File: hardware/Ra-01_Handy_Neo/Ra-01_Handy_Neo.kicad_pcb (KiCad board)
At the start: 2 copper layers, 68.6 x 53.3 mm, 11 parts, among them J1 Power, J2 Digital/PWM, J3 Analog, J4 Digital/PWM, J5 Conn_Coaxial, SW1 TVGP01-G73BB, U1 Ai-Thinker-Ra-01

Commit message: 80% done
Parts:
- removed MH1, MH2, MH3, MH4: MountingHole_3.2mm, Arduino_MountingHole:MountingHole_3.2mm
- added J6: Conn_01x04_Pin, Connector_PinHeader_2.54mm:PinHeader_1x04_P2.54mm_Horizontal, F.Cu at (110.9, 93.3)
- added R1: 10k, Resistor_SMD:R_0603_1608Metric_Pad0.98x0.95mm_HandSolder, F.Cu at (126.5, 84.5)
- added R10: 10k, Resistor_SMD:R_0603_1608Metric_Pad0.98x0.95mm_HandSolder, F.Cu at (161.0, 73.5)
- added R11: 10k, Resistor_SMD:R_0603_1608Metric_Pad0.98x0.95mm_HandSolder, F.Cu at (161.0, 84.5)
- added R12: 10k, Resistor_SMD:R_0603_1608Metric_Pad0.98x0.95mm_HandSolder, F.Cu at (165.0, 73.5)
- added R13: 10k, Resistor_SMD:R_0603_1608Metric_Pad0.98x0.95mm_HandSolder, F.Cu at (161.0, 62.0)
- added R2: 10k, Resistor_SMD:R_0603_1608Metric_Pad0.98x0.95mm_HandSolder, F.Cu at (126.5, 73.5)
- added R3: 10k, Resistor_SMD:R_0603_1608Metric_Pad0.98x0.95mm_HandSolder, F.Cu at (130.5, 73.5)
- added R4: 10k, Resistor_SMD:R_0603_1608Metric_Pad0.98x0.95mm_HandSolder, F.Cu at (138.0, 84.5)
- added R5: 10k, Resistor_SMD:R_0603_1608Metric_Pad0.98x0.95mm_HandSolder, F.Cu at (138.0, 73.5)
- added R6: 10k, Resistor_SMD:R_0603_1608Metric_Pad0.98x0.95mm_HandSolder, F.Cu at (142.0, 73.5)
- added R7: 10k, Resistor_SMD:R_0603_1608Metric_Pad0.98x0.95mm_HandSolder, F.Cu at (149.6, 84.5)
- added R8: 10k, Resistor_SMD:R_0603_1608Metric_Pad0.98x0.95mm_HandSolder, F.Cu at (149.5, 73.5)
- added R9: 10k, Resistor_SMD:R_0603_1608Metric_Pad0.98x0.95mm_HandSolder, F.Cu at (153.5, 73.5)
- added SW10: SW_Push, Button_Switch_THT:SW_PUSH_6mm_H5mm, F.Cu at (166.2, 81.0)
- added SW11: SW_Push, Button_Switch_THT:SW_PUSH_6mm_H5mm, F.Cu at (166.2, 91.8)
- added SW12: SW_Push, Button_Switch_THT:SW_PUSH_6mm_H5mm, F.Cu at (166.2, 69.8)
- added SW13: SW_Push, Button_Switch_THT:SW_PUSH_6mm_H5mm, F.Cu at (163.5, 58.5)
- added SW2: SW_Push, Button_Switch_THT:SW_PUSH_6mm_H5mm, F.Cu at (131.8, 81.0)
- added SW3: SW_Push, Button_Switch_THT:SW_PUSH_6mm_H5mm, F.Cu at (131.8, 69.8)
- added SW4: SW_Push, Button_Switch_THT:SW_PUSH_6mm_H5mm, F.Cu at (143.2, 91.8)
- added SW5: SW_Push, Button_Switch_THT:SW_PUSH_6mm_H5mm, F.Cu at (143.2, 81.0)
- added SW6: SW_Push, Button_Switch_THT:SW_PUSH_6mm_H5mm, F.Cu at (143.2, 69.8)
- added SW7: SW_Push, Button_Switch_THT:SW_PUSH_6mm_H5mm, F.Cu at (154.8, 91.8)
- added SW8: SW_Push, Button_Switch_THT:SW_PUSH_6mm_H5mm, F.Cu at (154.8, 81.0)
- added SW9: SW_Push, Button_Switch_THT:SW_PUSH_6mm_H5mm, F.Cu at (154.8, 69.8)
- added U2: TC74HC165AF, Package_SO:JEITA_SOIC-16_3.9x9.9mm_P1.27mm, B.Cu at (126.9, 57.4)
- added U3: TC74HC165AF, Package_SO:JEITA_SOIC-16_3.9x9.9mm_P1.27mm, B.Cu at (148.6, 57.4)
- SW1: value TVGP01-G73BB -> SW_Push; footprint Button_Switch_THT:SW_Tactile_12x12_TH_TVGP01-G73BB -> Button_Switch_THT:SW_PUSH_6mm_H5mm
- moved SW1 59.0 mm to (131.8, 91.8), turned to 180 degrees
- moved J5 43.3 mm to (105.0, 76.5), turned to 90 degrees
- moved U1 24.4 mm to (112.0, 62.0), turned to 90 degrees
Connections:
- J2 pad 1: /SCL/A5 -> SCL
- J2 pad 10: Ra_CS -> Ra_RESET
- J2 pad 2: /SDA/A4 -> SDA
- J2 pad 9: /*9 -> Ra_CS
- J3 pad 5: /SDA/A4 -> /A4
- J3 pad 6: /SCL/A5 -> /A5
- J4 pad 1: Ra_DIO5 -> SO
- J4 pad 2: Ra_DIO4 -> CP
- J4 pad 3: Ra_DIO3 -> ~{PL}
- J4 pad 4: Ra_DIO2 -> Ra_DIO0
- J4 pad 6: Ra_DIO0 -> Ra_DIO2
- SW1 pad 2: GND -> SW0
- U1 pad 10: Ra_DIO4 -> unconnected-(U1-DIO4-Pad10)
- U1 pad 11: Ra_DIO5 -> unconnected-(U1-DIO5-Pad11)
- U1 pad 8: Ra_DIO3 -> unconnected-(U1-DIO3-Pad8)
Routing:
- net +3V3: track 0.00 -> 64.1 mm, vias 0 -> 1
- net SW3: track 0.00 -> 57.2 mm
- net Ra_DIO2: track 0.00 -> 53.3 mm
- net Ra_DIO1: track 0.00 -> 53.0 mm
- net Ra_DIO0: track 0.00 -> 52.5 mm
- net SDA: track 0.00 -> 50.7 mm, vias 0 -> 1
- net SCL: track 0.00 -> 47.1 mm, vias 0 -> 1
- net SW6: track 0.00 -> 45.3 mm
- net Ra_RESET: track 0.00 -> 43.8 mm
- net SW7: track 0.00 -> 41.8 mm
- net Ra_CS: track 0.00 -> 40.7 mm
- net SW0: track 0.00 -> 38.9 mm
- net SWB: track 0.00 -> 35.0 mm
- net MOSI: track 0.00 -> 32.5 mm
- net SW4: track 0.00 -> 31.2 mm
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- added copper zone on In2.Cu, net +3V3
- added copper zone on In1.Cu, net GND
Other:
- copper layers 2 -> 4
- board text removed: "ICSP"

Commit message: koshin
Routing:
- net SW8: track 7.37 -> 17.6 mm
- net SW4: track 31.2 -> 34.3 mm
- net +3V3: track 64.1 -> 66.2 mm
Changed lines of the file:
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@@
 		(start 138.9125 73.5)
 		(end 141.0875 73.5)
-		(width 0.25)
+		(width 0.5)
 		(layer "F.Cu")
 		(net 23)
@@
 		(start 150.5 73.5875)
 		(end 150.4125 73.5)
-		(width 0.25)
+		(width 0.5)
 		(layer "F.Cu")
 		(net 23)
@@
 		(start 161.9125 62)
 		(end 161.9125 73.5)
-		(width 0.25)
+		(width 0.5)
 		(layer "F.Cu")
 		(net 23)
@@
 		(start 150.5 84.5)
 		(end 150.5 73.5875)
-		(width 0.25)
+		(width 0.5)
+		(layer "F.Cu")
+		(net 23)
+	)
+	(segment
+		(start 150.4125 73.5)
+		(end 152.5875 73.5)
+		(width 0.5)
 		(layer "F.Cu")
 		(net 23)
@@
 		(start 138.9125 84.5)
 		(end 138.9125 73.5)
-		(width 0.25)
+		(width 0.5)
 		(layer "F.Cu")
 		(net 23)
@@
 		(start 161.9125 84.5)
 		(end 161.9125 73.5)
-		(width 0.25)
+		(width 0.5)
 		(layer "F.Cu")
 		(net 23)
@@
 		(start 161.9125 73.5)
 		(end 164.0875 73.5)
-		(width 0.25)
+		(width 0.5)
 		(layer "F.Cu")
 		(net 23)
@@
 		(start 127.4125 73.5)
 		(end 127.4125 84.5)
-		(width 0.25)
+		(width 0.5)
 		(layer "F.Cu")
 		(net 23)
@@
 		(start 127.4125 73.5)
 		(end 129.5875 73.5)
-		(width 0.25)
+		(width 0.5)
 		(layer "F.Cu")
 		(net 23)
@@
 		(start 145.5 67.5)
 		(end 143.25 65.25)
-		(width 0.25)
+		(width 0.3)
 		(layer "F.Cu")
 		(net 32)
@@
 		(start 142.9125 73.5)
 		(end 145.5 70.9125)
-		(width 0.25)
+		(width 0.3)
 		(layer "F.Cu")
 		(net 32)
@@
 		(start 145.5 70.9125)
 		(end 145.5 67.5)
-		(width 0.25)
+		(width 0.3)
 		(layer "F.Cu")
 		(net 32)
@@
 		(start 125.25 87.25)
 		(end 125.5875 86.9125)
-		(width 0.25)
+		(width 0.3)
 		(layer "F.Cu")
 		(net 33)
@@
 		(start 125.5875 86.9125)
 		(end 125.5875 84.5)
-		(width 0.25)
+		(width 0.3)
 		(layer "F.Cu")
 		(net 33)
@@
 		(start 148.5875 76.1625)
 		(end 148.25 76.5)
-		(width 0.25)
+		(width 0.3)
 		(layer "F.Cu")
 		(net 34)
@@
 		(start 148.5875 73.5)
 		(end 148.5875 76.1625)
-		(width 0.25)
+		(width 0.3)
 		(layer "F.Cu")
 		(net 34)
@@
 		(start 125.5875 73.5)
 		(end 125.5875 76.1625)
-		(width 0.25)
+		(width 0.3)
 		(layer "F.Cu")
 		(net 35)
@@
 		(start 125.5875 76.1625)
 		(end 125.25 76.5)
-		(width 0.25)
+		(width 0.3)
 		(layer "F.Cu")
 		(net 35)
@@
 		(start 134 67.5)
 		(end 131.75 65.25)
-		(width 0.25)
+		(width 0.3)
 		(layer "F.Cu")
 		(net 37)
@@
 		(start 131.4125 73.5)
 		(end 134 70.9125)
-		(width 0.25)
+		(width 0.3)
 		(layer "F.Cu")
 		(net 37)
@@
 		(start 134 70.9125)
 		(end 134 67.5)
-		(width 0.25)
+		(width 0.3)
 		(layer "F.Cu")
 		(net 37)
@@
 		(start 137.0875 86.9125)
 		(end 136.75 87.25)
-		(width 0.25)
+		(width 0.3)
 		(layer "F.Cu")
 		(net 38)
@@
 		(start 137.0875 84.5)
 		(end 137.0875 86.9125)
-		(width 0.25)
+		(width 0.3)
 		(layer "F.Cu")
 		(net 38)
@@
 	)
 	(segment
+		(start 137.0875 73.5)
+		(end 137.0875 76.1625)
+		(width 0.3)
+		(layer "F.Cu")
+		(net 40)
+	)
+	(segment
+		(start 137.0875 76.1625)
+		(end 136.75 76.5)
+		(width 0.3)
+		(layer "F.Cu")
+		(net 40)
+	)
+	(segment
 		(start 129.725 55.46)
 		(end 137.46 55.46)
@@
 		(start 148.675 86.825)
 		(end 148.25 87.25)
-		(width 0.25)
+		(width 0.3)
 		(layer "F.Cu")
 		(net 41)
@@
 		(start 148.675 84.5)
 		(end 148.675 86.825)
-		(width 0.25)
+		(width 0.3)
 		(layer "F.Cu")
 		(net 41)
@@
 		(start 160.0875 84.5)
 		(end 160.0875 86.9125)
-		(width 0.25)
+		(width 0.3)
 		(layer "F.Cu")
 		(net 42)
@@
 		(start 160.0875 86.9125)
 		(end 159.75 87.25)
-		(width 0.25)
+		(width 0.3)
 		(layer "F.Cu")
 		(net 42)
@@
 	)
 	(segment
+		(start 168 67)
+		(end 166.25 65.25)
+		(width 0.3)
+		(layer "F.Cu")
+		(net 43)
+	)
+	(segment
+		(start 165.9125 73.5)
+		(end 168 71.4125)
+		(width 0.3)
+		(layer "F.Cu")
+		(net 43)
+	)
+	(segment
 		(start 168 71.4125)
 		(end 168 67)
-		(width 0.25)
-		(layer "F.Cu")
-		(net 43)
-	)
-	(segment
-		(start 168 67)
-		(end 166.25 65.25)
-		(width 0.25)
-		(layer "F.Cu")
-		(net 43)
-	)
-	(segment
-		(start 165.9125 73.5)
-		(end 168 71.4125)
-		(width 0.25)
+		(width 0.3)
 		(layer "F.Cu")
 		(net 43)
@@
 		(start 160.0875 62)
 		(end 160.0875 57.0875)
-		(width 0.25)
+		(width 0.3)
 		(layer "F.Cu")
 		(net 44)
@@
 		(start 160.0875 57.0875)
 		(end 157 54)
-		(width 0.25)
+		(width 0.3)
 		(layer "F.Cu")
 		(net 44)
@@
 	)
 	(segment
+		(start 157 67.5)
+		(end 154.75 65.25)
+		(width 0.3)
+		(layer "F.Cu")
+		(net 46)
+	)
+	(segment
+		(start 154.4125 73.5)
+		(end 157 70.9125)
+		(width 0.3)
+		(layer "F.Cu")
+		(net 46)
+	)
+	(segment
+		(start 157 70.9125)
+		(end 157 67.5)
+		(width 0.3)
+		(layer "F.Cu")
+		(net 46)
+	)
+	(segment
 		(start 146.391249 59.27)
 		(end 148 60.878751)
@@
 		(start 160.0875 73.5)
 		(end 160.0875 76.1625)
-		(width 0.25)
+		(width 0.3)
 		(layer "F.Cu")
 		(net 47)
@@
 		(start 160.0875 76.1625)
 		(end 159.75 76.5)
-		(width 0.25)
+		(width 0.3)
 		(layer "F.Cu")
 		(net 47)

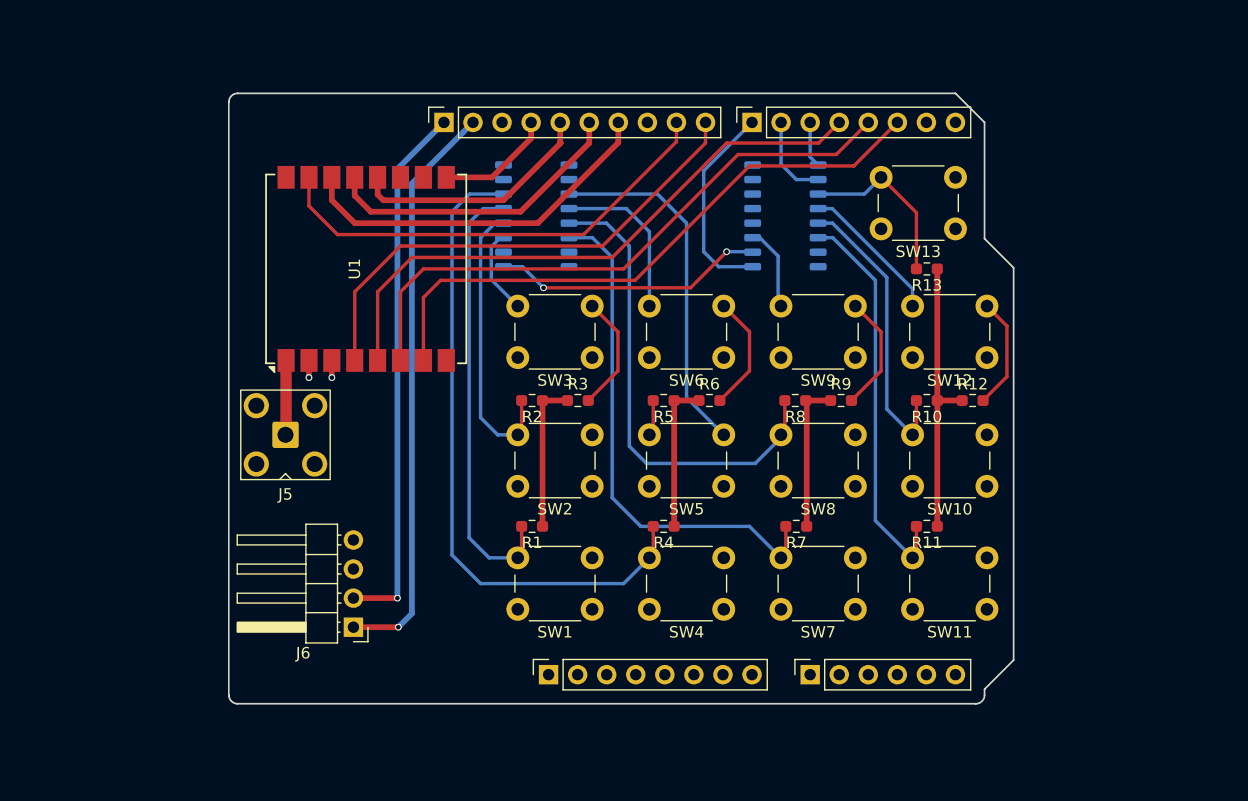
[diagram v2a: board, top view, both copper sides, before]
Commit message: pcb almost complete
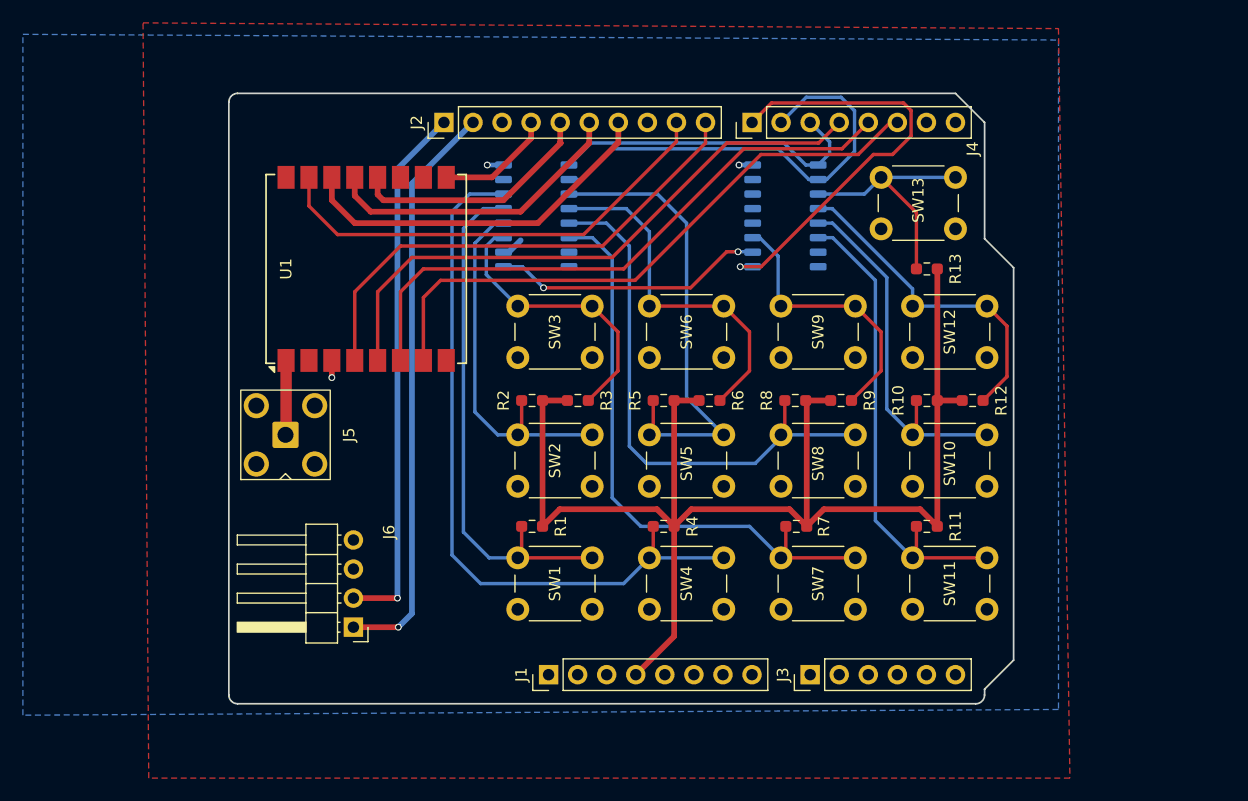
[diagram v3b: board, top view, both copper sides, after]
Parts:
- J1, J4: footprint Connector_PinSocket_2.54mm:PinSocket_1x08_P2.54mm_Vertical -> Connector_PinHeader_2.54mm:PinHeader_1x08_P2.54mm_Vertical
- J2: footprint Connector_PinSocket_2.54mm:PinSocket_1x10_P2.54mm_Vertical -> Connector_PinHeader_2.54mm:PinHeader_1x10_P2.54mm_Vertical
- J3: footprint Connector_PinSocket_2.54mm:PinSocket_1x06_P2.54mm_Vertical -> Connector_PinHeader_2.54mm:PinHeader_1x06_P2.54mm_Vertical
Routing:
- net +3V3: track 66.2 -> 121.4 mm, vias 1 -> 3
- net CP: track 7.45 -> 39.6 mm
- net ~{PL}: track 4.01 -> 28.2 mm
- net SO: track 17.9 -> 37.8 mm, vias 0 -> 1
- net SW2: track 17.8 -> 24.9 mm
- net SW0: track 38.9 -> 45.8 mm
- net SW1: track 25.3 -> 32.2 mm
- net SW7: track 41.8 -> 48.3 mm
- net SWS: track 15.4 -> 21.9 mm
- net SWE: track 22.5 -> 29.0 mm
- net SWB: track 35.0 -> 41.5 mm
- net SW6: track 45.3 -> 51.8 mm
- net SW5: track 24.6 -> 31.1 mm
- net SW4: track 34.3 -> 40.8 mm
- net SW3: track 57.2 -> 63.7 mm
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- added copper zone on B.Cu, net GND
- added copper zone on F.Cu, net GND
